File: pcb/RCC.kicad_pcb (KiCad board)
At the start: 2 copper layers, 25.4 x 25.4 mm, 15 parts, among them SW1 SW_MEC_5E, U1 ATtiny402-SS

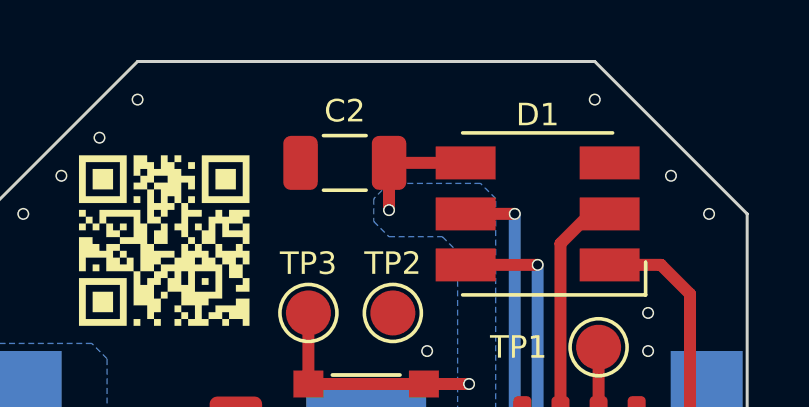
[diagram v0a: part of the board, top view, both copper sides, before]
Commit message: Add text variables to pcb
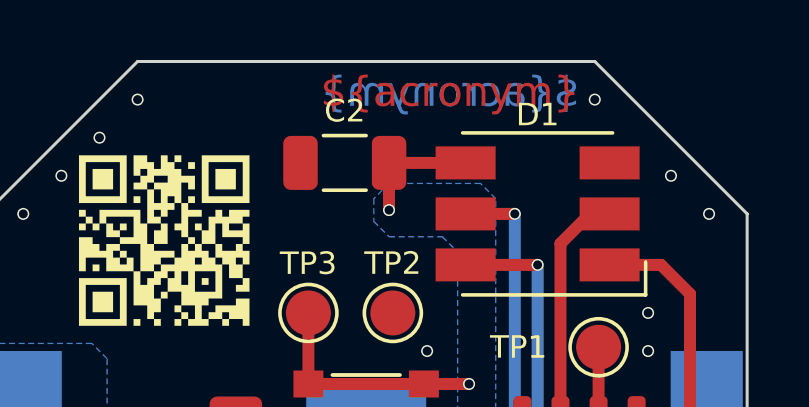
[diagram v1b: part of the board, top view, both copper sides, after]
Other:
- board text added: "${acronym}"
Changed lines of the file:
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@@
   )
   (paper "A4")
+  (title_block
+    (title "${acronym} - ${title}")
+    (date "${date}")
+    (rev "${revision}")
+    (company "${company}")
+    (comment 1 "${creator}")
+    (comment 2 "${license}")
+  )
   (layers
     (0 "F.Cu" signal)
@@
   (gr_line (start 165.1 76.2) (end 170.18 81.28)
     (stroke (width 0.1) (type default)) (layer "Edge.Cuts"))
+  (gr_text "${acronym}" (at 160.274 77.216) (layer "F.Cu")
+    (effects (font (size 1 1) (thickness 0.15)))
+  )
+  (gr_text "${acronym}" (at 160.274 77.216) (layer "B.Cu")
+    (effects (font (size 1 1) (thickness 0.15)) (justify mirror))
+  )
   (gr_text "Test:" (at 156.972 80.518) (layer "B.SilkS")
     (effects (font (size 0.5 0.5) (thickness 0.1) bold) (justify left mirror))
